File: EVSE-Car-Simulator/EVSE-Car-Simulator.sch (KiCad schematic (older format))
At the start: 11 parts, among them J1 diode fault, J2 vehicle detected, J3 CP short circuit, J4 vehicle ready, J5 Typ 2 Stecker, J6 CP diag, J7 PE diag

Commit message: completely routed, gerber files for production generated.
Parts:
- D1: value D -> 1N4007
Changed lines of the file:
@@
 P 1800 2150
 F 0 "D1" H 1800 2250 50  0000 C CNN
-F 1 "D" H 1800 2050 50  0000 C CNN
+F 1 "1N4007" H 1800 2050 50  0000 C CNN
 F 2 "Diodes_THT:D_DO-41_SOD81_P7.62mm_Horizontal" H 1800 2150 50  0001 C CNN
 F 3 "" H 1800 2150 50  0001 C CNN

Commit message: added images
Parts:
- R1, R2, R3: symbol R -> R-RESCUE-EVSE-Car-Simulator
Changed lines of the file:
@@
 EESchema Schematic File Version 2
+LIBS:EVSE-Car-Simulator-rescue
 LIBS:power
 LIBS:device
@@
 $EndDescr
 $Comp
-L R R2
+L R-RESCUE-EVSE-Car-Simulator R2
 U 1 1 59A9487E
 P 4050 5550
@@
 	7200 2150 7050 2150
 $Comp
-L R R3
+L R-RESCUE-EVSE-Car-Simulator R3
 U 1 1 59A94F9B
 P 8750 2300
@@
 CP
 $Comp
-L R R1
+L R-RESCUE-EVSE-Car-Simulator R1
 U 1 1 59A954A9
 P 2150 5500

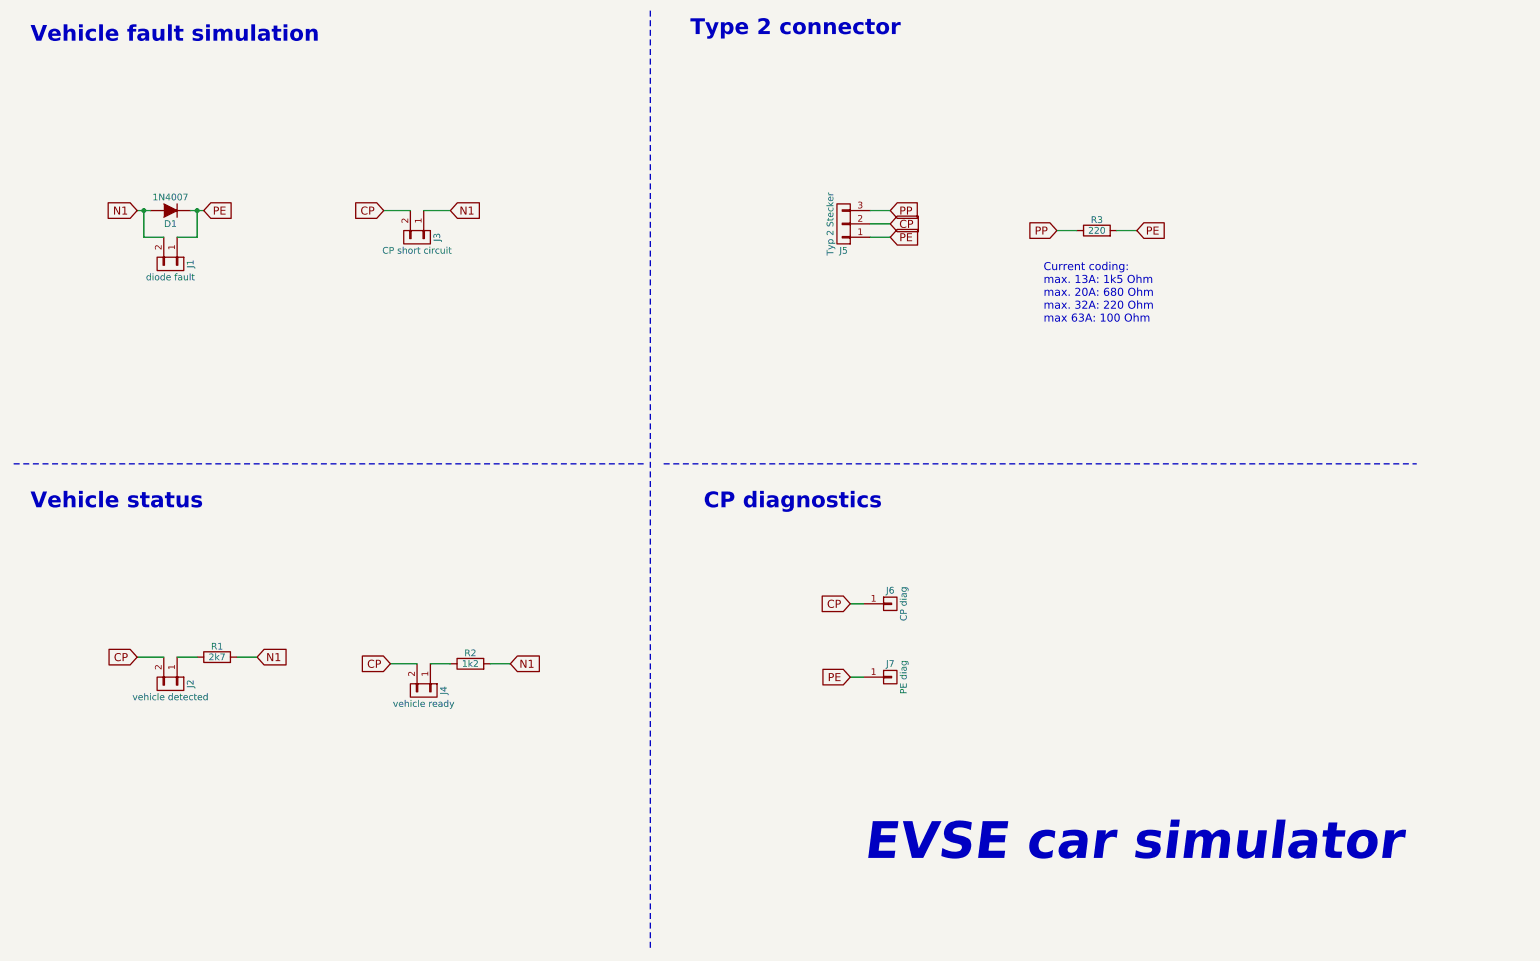
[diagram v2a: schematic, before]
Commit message: increased hole size for type2 connector, rerouted to make enough room
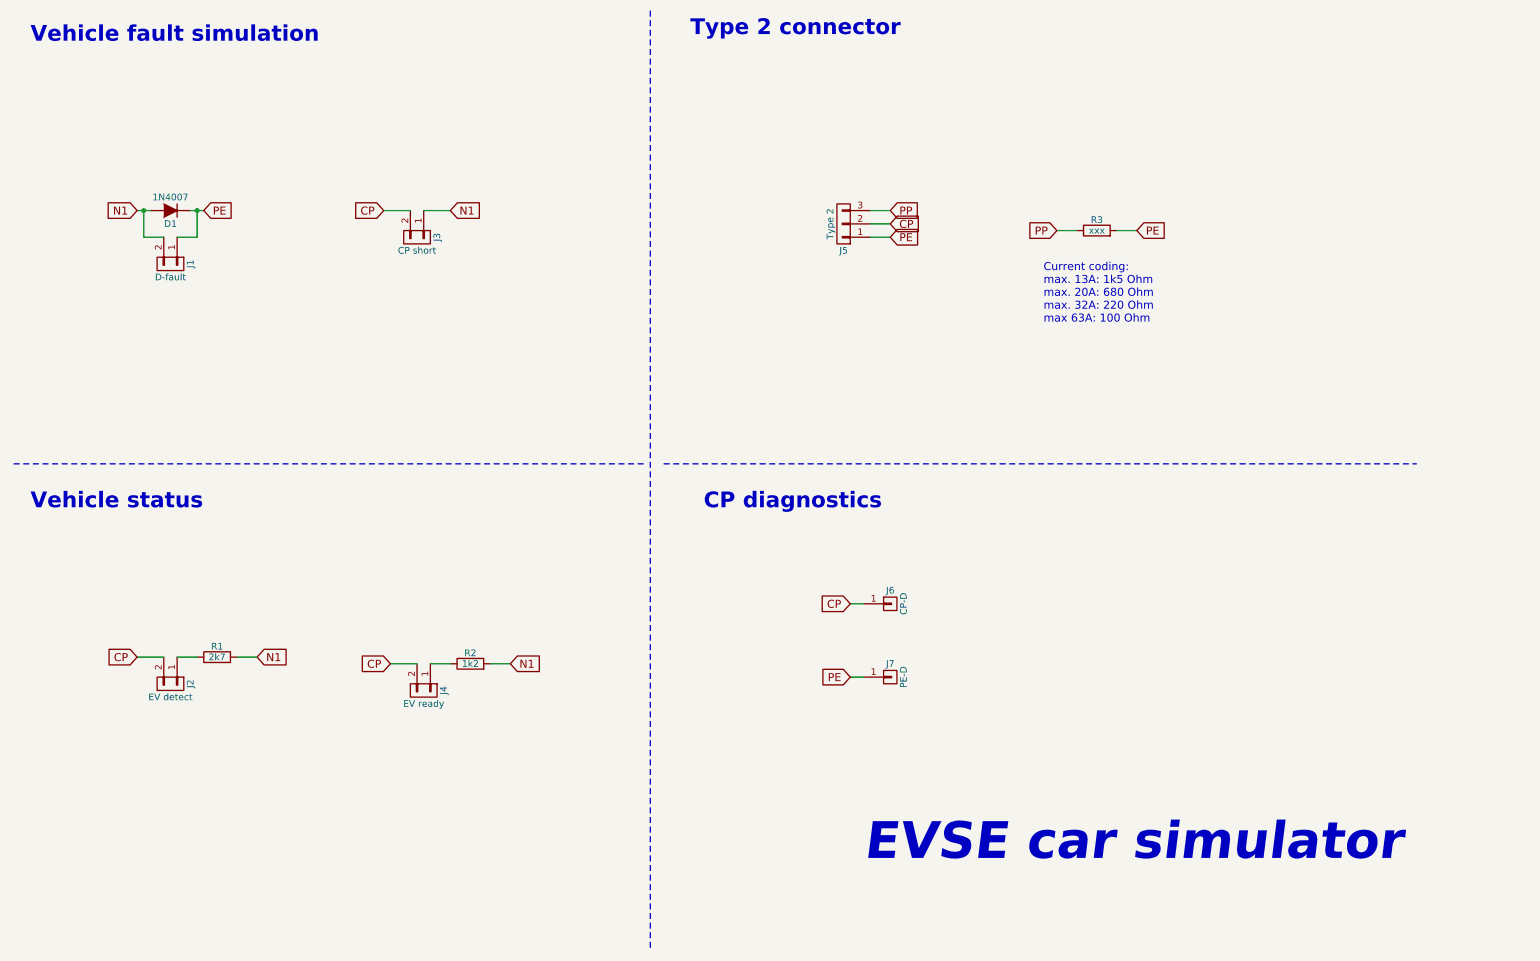
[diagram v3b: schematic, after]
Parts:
- J1: value diode fault -> D-fault
- J2: value vehicle detected -> EV detect
- J3: value CP short circuit -> CP short
- J4: value vehicle ready -> EV ready
- J5: value Typ 2 Stecker -> Type 2; footprint Pin_Headers:Pin_Header_Straight_1x03_Pitch2.54mm -> lib:Type2-Solderpads
- J6: value CP diag -> CP-D
- J7: value PE diag -> PE-D
- R3: value 220 -> xxx
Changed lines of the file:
@@
 P 3700 5750
 F 0 "J4" H 3700 5900 50  0000 C CNN
-F 1 "vehicle ready" V 3800 5750 50  0000 C CNN
+F 1 "EV ready" V 3800 5750 50  0000 C CNN
 F 2 "Pin_Headers:Pin_Header_Straight_1x02_Pitch2.54mm" H 3700 5750 50  0001 C CNN
 F 3 "" H 3700 5750 50  0001 C CNN
@@
 P 6850 2250
 F 0 "J5" H 6850 2450 50  0000 C CNN
-F 1 "Typ 2 Stecker" V 6950 2250 50  0000 C CNN
-F 2 "Pin_Headers:Pin_Header_Straight_1x03_Pitch2.54mm" H 6850 2250 50  0001 C CNN
+F 1 "Type 2" V 6950 2250 50  0000 C CNN
+F 2 "lib:Type2-Solderpads" H 6850 2250 50  0001 C CNN
 F 3 "" H 6850 2250 50  0001 C CNN
 	1    6850 2250
@@
 P 8750 2300
 F 0 "R3" V 8830 2300 50  0000 C CNN
-F 1 "220" V 8750 2300 50  0000 C CNN
+F 1 "xxx" V 8750 2300 50  0000 C CNN
 F 2 "Resistors_THT:R_Axial_DIN0204_L3.6mm_D1.6mm_P7.62mm_Horizontal" V 8680 2300 50  0001 C CNN
 F 3 "" H 8750 2300 50  0001 C CNN
@@
 P 1800 5700
 F 0 "J2" H 1800 5850 50  0000 C CNN
-F 1 "vehicle detected" V 1900 5700 50  0000 C CNN
+F 1 "EV detect" V 1900 5700 50  0000 C CNN
 F 2 "Pin_Headers:Pin_Header_Straight_1x02_Pitch2.54mm" H 1800 5700 50  0001 C CNN
 F 3 "" H 1800 5700 50  0001 C CNN
@@
 P 1800 2550
 F 0 "J1" H 1800 2700 50  0000 C CNN
-F 1 "diode fault" V 1900 2550 50  0000 C CNN
+F 1 "D-fault" V 1900 2550 50  0000 C CNN
 F 2 "Pin_Headers:Pin_Header_Straight_1x02_Pitch2.54mm" H 1800 2550 50  0001 C CNN
 F 3 "" H 1800 2550 50  0001 C CNN
@@
 P 3650 2350
 F 0 "J3" H 3650 2500 50  0000 C CNN
-F 1 "CP short circuit" V 3750 2350 50  0000 C CNN
+F 1 "CP short" V 3750 2350 50  0000 C CNN
 F 2 "Pin_Headers:Pin_Header_Straight_1x02_Pitch2.54mm" H 3650 2350 50  0001 C CNN
 F 3 "" H 3650 2350 50  0001 C CNN
@@
 P 7200 5100
 F 0 "J6" H 7200 5200 50  0000 C CNN
-F 1 "CP diag" V 7300 5100 50  0000 C CNN
+F 1 "CP-D" V 7300 5100 50  0000 C CNN
 F 2 "Pin_Headers:Pin_Header_Straight_1x01_Pitch2.54mm" H 7200 5100 50  0001 C CNN
 F 3 "" H 7200 5100 50  0001 C CNN
@@
 P 7200 5650
 F 0 "J7" H 7200 5750 50  0000 C CNN
-F 1 "PE diag" V 7300 5650 50  0000 C CNN
+F 1 "PE-D" V 7300 5650 50  0000 C CNN
 F 2 "Pin_Headers:Pin_Header_Straight_1x01_Pitch2.54mm" H 7200 5650 50  0001 C CNN
 F 3 "" H 7200 5650 50  0001 C CNN

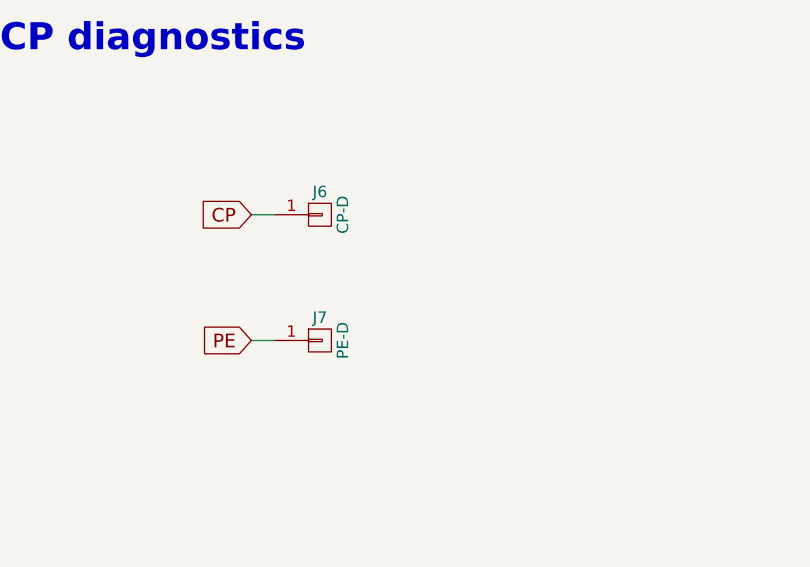
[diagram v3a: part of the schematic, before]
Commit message: changed connector of test lines
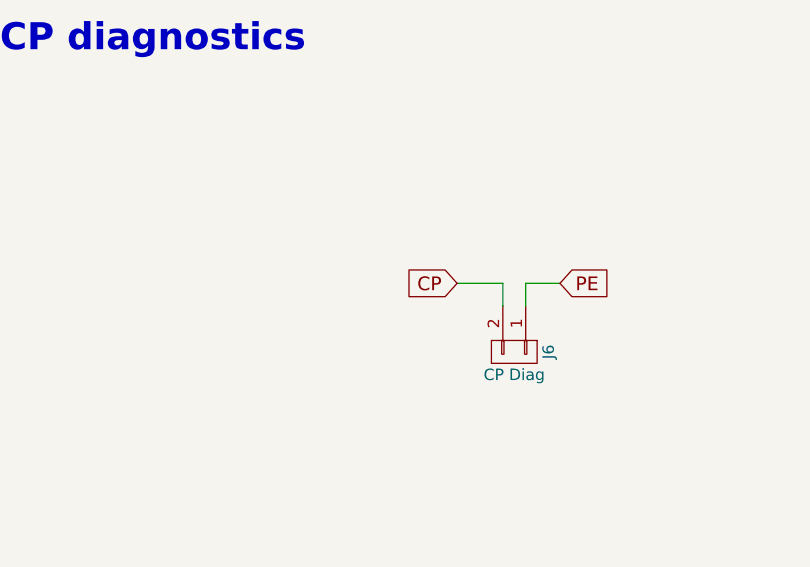
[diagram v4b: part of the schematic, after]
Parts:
- removed J6: CP-D, Pin_Headers:Pin_Header_Straight_1x01_Pitch2.54mm, symbol CONN_01X01
- removed J7: PE-D, Pin_Headers:Pin_Header_Straight_1x01_Pitch2.54mm, symbol CONN_01X01
- added J6: CP Diag, Pin_Headers:Pin_Header_Straight_1x02_Pitch2.54mm, symbol CONN_01X02
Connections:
- net CP: now also J6.2 (P2)
- net PE: now also J6.1 (P1)
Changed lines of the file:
@@
 Sheet 1 1
 Title "Car simulator"
-Date "2017-09-01"
-Rev "0.1"
+Date "2018-01-09"
+Rev "0.3"
 Comp ""
 Comment1 ""
@@
 Wire Notes Line
 	5500 4050 11150 4050
-Text GLabel 6900 5100 0    60   Input ~ 0
-CP
-Text GLabel 6900 5650 0    60   Input ~ 0
-PE
-$Comp
-L CONN_01X01 J6
-U 1 1 59A9695E
-P 7200 5100
-F 0 "J6" H 7200 5200 50  0000 C CNN
-F 1 "CP-D" V 7300 5100 50  0000 C CNN
-F 2 "Pin_Headers:Pin_Header_Straight_1x01_Pitch2.54mm" H 7200 5100 50  0001 C CNN
-F 3 "" H 7200 5100 50  0001 C CNN
-	1    7200 5100
-	1    0    0    -1
-$EndComp
-$Comp
-L CONN_01X01 J7
-U 1 1 59A969B7
-P 7200 5650
-F 0 "J7" H 7200 5750 50  0000 C CNN
-F 1 "PE-D" V 7300 5650 50  0000 C CNN
-F 2 "Pin_Headers:Pin_Header_Straight_1x01_Pitch2.54mm" H 7200 5650 50  0001 C CNN
-F 3 "" H 7200 5650 50  0001 C CNN
-	1    7200 5650
-	1    0    0    -1
-$EndComp
-Wire Wire Line
-	6900 5650 7000 5650
-Wire Wire Line
-	7000 5100 6900 5100
+Text GLabel 7800 5400 0    60   Input ~ 0
+CP
+Text GLabel 8250 5400 2    60   Input ~ 0
+PE
 Text Notes 7000 7050 0    276  Italic 55
 EVSE car simulator
+$Comp
+L CONN_01X02 J6
+U 1 1 5A5523CA
+P 8050 5700
+F 0 "J6" H 8050 5850 50  0000 C CNN
+F 1 "CP Diag" V 8150 5700 50  0000 C CNN
+F 2 "Pin_Headers:Pin_Header_Straight_1x02_Pitch2.54mm" H 8050 5700 50  0001 C CNN
+F 3 "" H 8050 5700 50  0001 C CNN
+	1    8050 5700
+	0    1    1    0
+$EndComp
+Wire Wire Line
+	7800 5400 8000 5400
+Wire Wire Line
+	8000 5400 8000 5500
+Wire Wire Line
+	8100 5500 8100 5400
+Wire Wire Line
+	8100 5400 8250 5400
 $EndSCHEMATC
